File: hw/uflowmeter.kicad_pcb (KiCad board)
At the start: 4 copper layers, 70 x 55 mm, 32 parts, among them J1 SBW, J3 Display, J4 Transducers, J5 Cal UART, J6 Radio module, Q1 IRLML6401, SW1 Button, U1 MSP430FR5043IRGC, Y1 32.768kHz, Y2 8MHz

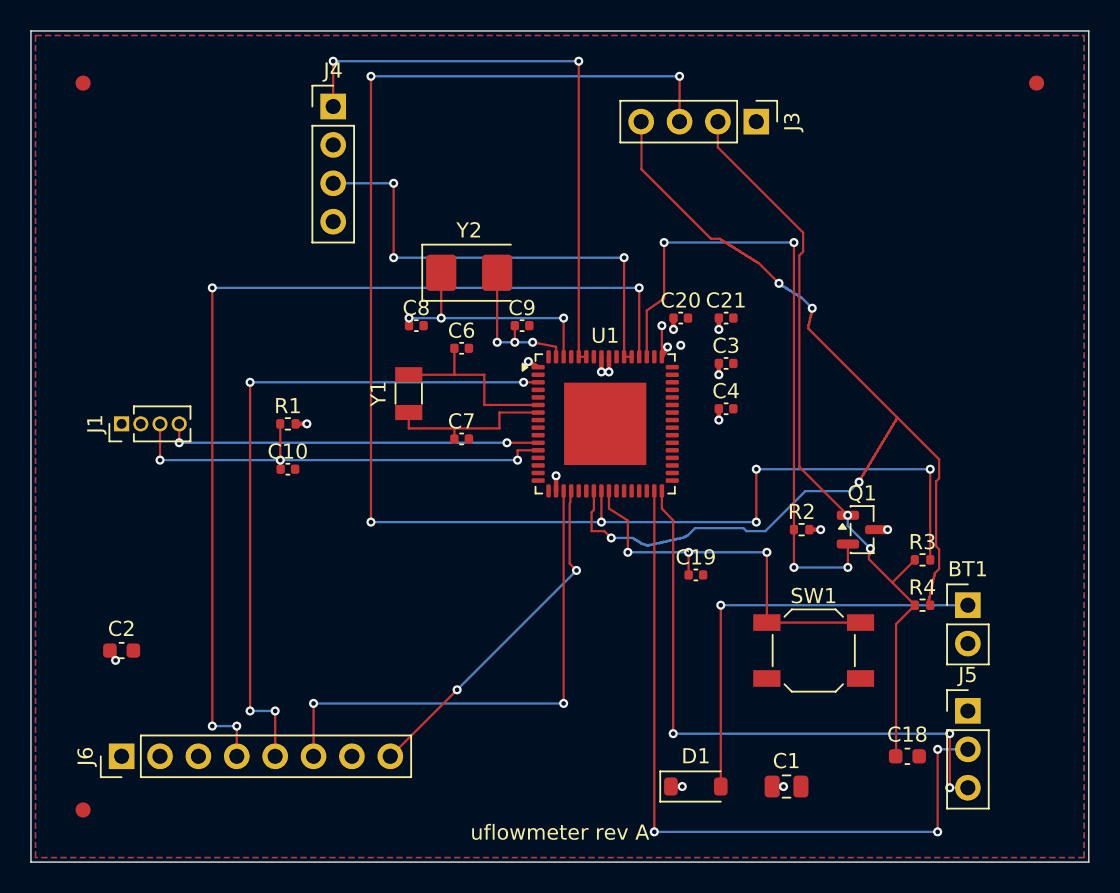
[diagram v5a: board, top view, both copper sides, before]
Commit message: hw: every track on the 0/45/90 grid
The angle histogram is now 0, 45, 90 and 135 and nothing else. Three fixes,
none of them in the routing proper.

The fan escapes had arbitrary slopes. A fan separates two adjacent pins'
escapes, and its sideways step and downward step have to be equal for the
diagonal to come out at 45 degrees; setting them independently gave 11, 10,
15 and 1.8 degrees.

The supply stitcher stepped its candidate vias round the pad in 30 degrees,
so the stub between pad and via landed at 60. Multiples of 45 only now. That
edit had been attempted once before by pattern replacement and silently did
not apply -- the numbers gave it away, 0.375 and 0.65 over a length of 0.75
being exactly cos and sin of sixty.

And USSXTOUT escaped 0.16 mm before turning, which was too little: the
diagonal ran alongside USSXTIN's pad, the cleanup pass removed it as a
clearance violation, and the next router built a detour at whatever angle
suited it. One cause behind three symptoms -- a crooked track, copper nobody
asked for, and a broken connection. Both crystal nets are redrawn: USSXTOUT
stays on the top layer throughout, since Y2 and C9 are both surface mount and
millimetres away, and it reaches C9.1 from above because a run along y=19.5
would cross that capacitor's ground pad.

mitre_corners.py chamfers square corners where it is safe: not within 0.6 mm
of a pad or via, not on legs under 1 mm, never more than 30 % of the shorter
leg. A bolder version cut corners into neighbouring lanes for 17 violations,
the lane spacing having been worked out for orthogonal runs. Right angles
that survive are left alone -- a right angle in a track is not a
manufacturing problem, the acid trap is about acute angles.

189 tracks, 66 vias. Zero DRC violations, zero unconnected, ERC clean,
nothing off-grid, nothing over 2.5x its floor.

Co-Authored-By: Claude Opus 5 (1M context) <noreply@anthropic.com>
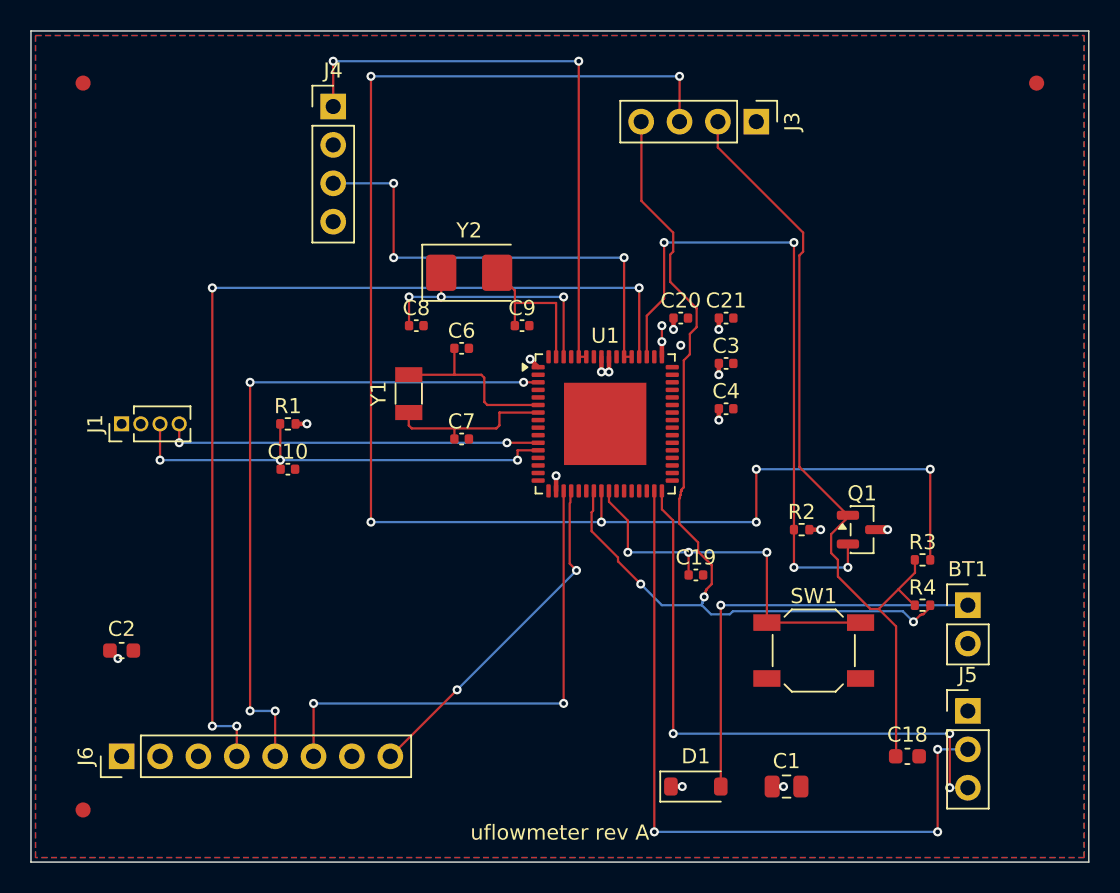
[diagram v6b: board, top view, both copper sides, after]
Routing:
- net I2C_SDA: track 69.8 -> 63.4 mm, vias 4 -> 3
- net VCC_DISP: track 49.6 -> 53.4 mm, vias 2 -> 0
- net USSXTIN: track 16.3 -> 17.7 mm
- net USSXTOUT: vias 3 -> 0
